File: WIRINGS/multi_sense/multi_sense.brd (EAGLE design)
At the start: 45.7 x 62.2 mm, 7 parts

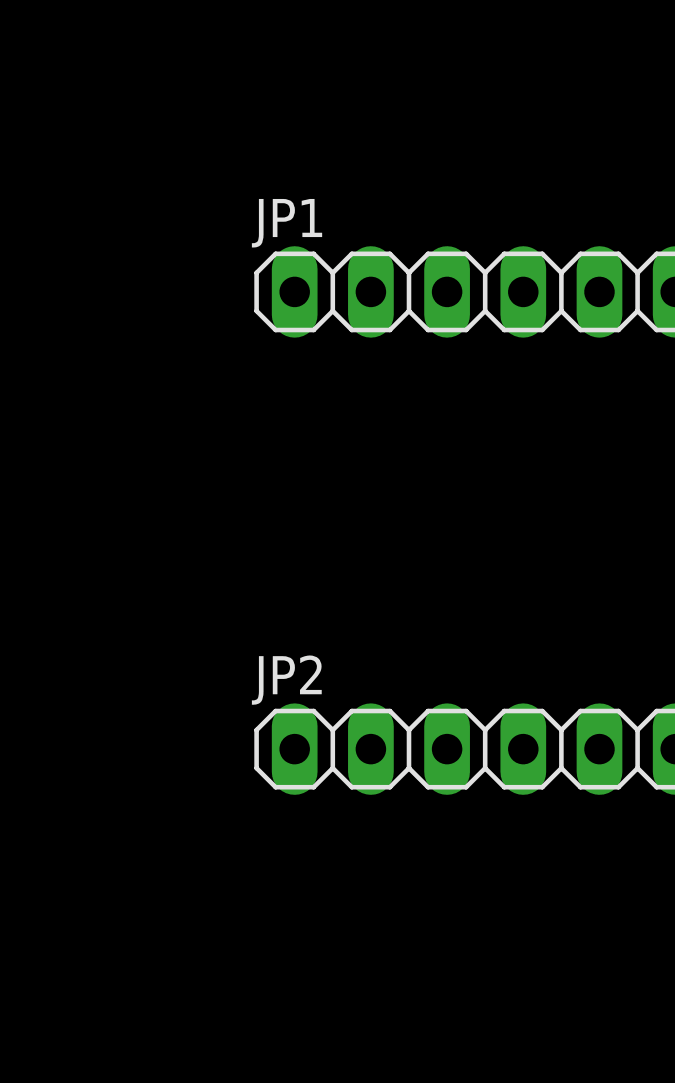
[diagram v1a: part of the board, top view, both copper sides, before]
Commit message: updated wemos and diverse boards
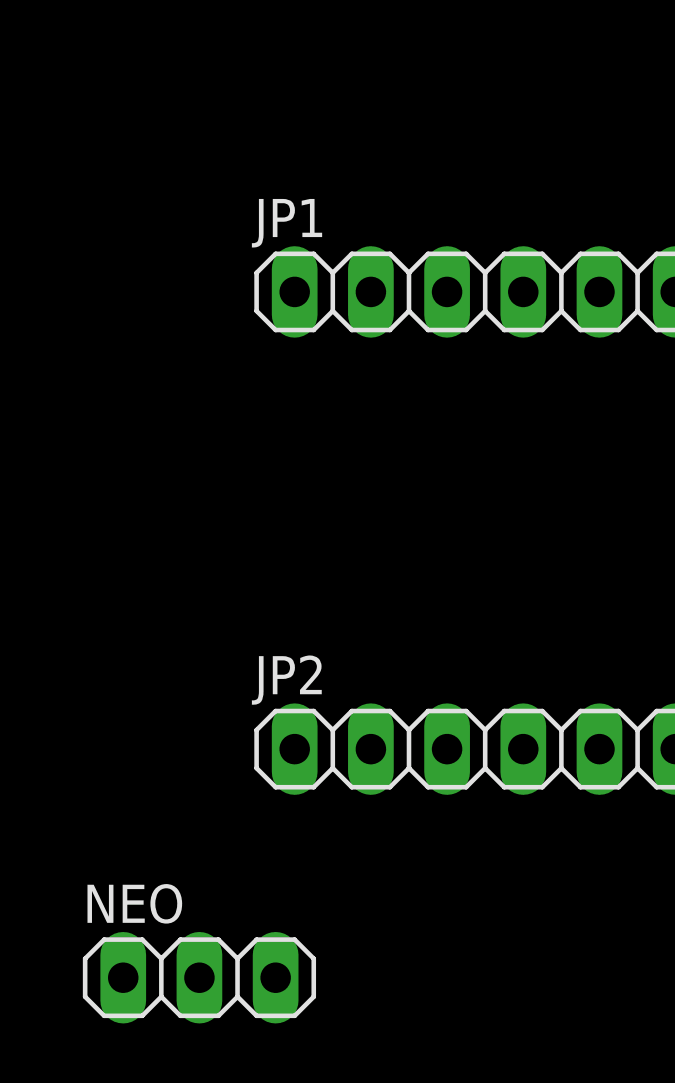
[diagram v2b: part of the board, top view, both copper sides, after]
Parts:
- added NEO: (no value), pinhead:1X03
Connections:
- new net NEOGND: NEO.2
- new net NEOPWR: NEO.3
- new net NEOSIG: NEO.1
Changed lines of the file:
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@@
 <?xml version="1.0" encoding="utf-8"?>
 <!DOCTYPE eagle SYSTEM "eagle.dtd">
-<eagle version="8.3.2">
+<eagle version="9.6.2">
 <drawing>
 <settings>
@@
 <param name="dpMaxLengthDifference" value="10mm"/>
 <param name="dpGapFactor" value="2.5"/>
-<param name="checkGrid" value="0"/>
 <param name="checkAngle" value="0"/>
 <param name="checkFont" value="1"/>
 <param name="checkRestrict" value="0"/>
+<param name="checkStop" value="0"/>
+<param name="checkValues" value="0"/>
+<param name="checkNames" value="1"/>
+<param name="checkWireStubs" value="1"/>
+<param name="checkPolygonWidth" value="0"/>
 <param name="useDiameter" value="13"/>
 <param name="maxErrors" value="50"/>
@@
 </autorouter>
 <elements>
-<element name="U$2" library="BRAND_SWI" package="BRAND_SWI_5X7" value="" x="11.303" y="0.635" rot="MR0"/>
-<element name="R1" library="rcl" library_urn="urn:adsk.eagle:library:334" package="0207/10" package3d_urn="urn:adsk.eagle:package:23491/1" value="10k" x="10.795" y="-130.81"/>
-<element name="PIR" library="pinhead" library_urn="urn:adsk.eagle:library:325" package="1X03" package3d_urn="urn:adsk.eagle:package:22458/2" value="" x="10.16" y="-290.83"/>
-<element name="DHT" library="pinhead" library_urn="urn:adsk.eagle:library:325" package="1X04" package3d_urn="urn:adsk.eagle:package:22407/2" value="" x="11.43" y="-306.07"/>
-<element name="TEMT6000" library="pinhead" library_urn="urn:adsk.eagle:library:325" package="1X03" package3d_urn="urn:adsk.eagle:package:22458/2" value="" x="10.16" y="-321.31"/>
-<element name="JP1" library="pinhead" library_urn="urn:adsk.eagle:library:325" package="1X15" package3d_urn="urn:adsk.eagle:package:22424/1" value="ESP8266_LEFT" x="25.4" y="-336.55"/>
-<element name="JP2" library="pinhead" library_urn="urn:adsk.eagle:library:325" package="1X15" package3d_urn="urn:adsk.eagle:package:22424/1" value="ESP8266_LEFT" x="25.4" y="-351.79"/>
+<element name="U$2" library="BRAND_SWI" package="BRAND_SWI_5X7" value="" x="11.303" y="0.635" smashed="yes" rot="MR0"/>
+<element name="R1" library="rcl" library_urn="urn:adsk.eagle:library:334" package="0207/10" package3d_urn="urn:adsk.eagle:package:23491/1" value="10k" x="10.795" y="-130.81" smashed="yes">
+<attribute name="NAME" x="7.747" y="-129.286" size="1.27" layer="25" ratio="10"/>
+<attribute name="VALUE" x="8.5344" y="-131.445" size="1.27" layer="27" ratio="10"/>
+</element>
+<element name="PIR" library="pinhead" library_urn="urn:adsk.eagle:library:325" package="1X03" package3d_urn="urn:adsk.eagle:package:22458/2" value="" x="10.16" y="-290.83" smashed="yes">
+<attribute name="NAME" x="6.2738" y="-289.0012" size="1.27" layer="25" ratio="10"/>
+<attribute name="VALUE" x="6.35" y="-294.005" size="1.27" layer="27"/>
+</element>
+<element name="DHT" library="pinhead" library_urn="urn:adsk.eagle:library:325" package="1X04" package3d_urn="urn:adsk.eagle:package:22407/2" value="" x="11.43" y="-306.07" smashed="yes">
+<attribute name="NAME" x="6.2738" y="-304.2412" size="1.27" layer="25" ratio="10"/>
+<attribute name="VALUE" x="6.35" y="-309.245" size="1.27" layer="27"/>
+</element>
+<element name="TEMT6000" library="pinhead" library_urn="urn:adsk.eagle:library:325" package="1X03" package3d_urn="urn:adsk.eagle:package:22458/2" value="" x="10.16" y="-321.31" smashed="yes">
+<attribute name="NAME" x="6.2738" y="-319.4812" size="1.27" layer="25" ratio="10"/>
+<attribute name="VALUE" x="6.35" y="-324.485" size="1.27" layer="27"/>
+</element>
+<element name="JP1" library="pinhead" library_urn="urn:adsk.eagle:library:325" package="1X15" package3d_urn="urn:adsk.eagle:package:22424/1" value="ESP8266_LEFT" x="25.4" y="-336.55" smashed="yes">
+<attribute name="NAME" x="6.2738" y="-334.7212" size="1.27" layer="25" ratio="10"/>
+<attribute name="VALUE" x="6.35" y="-339.725" size="1.27" layer="27"/>
+</element>
+<element name="JP2" library="pinhead" library_urn="urn:adsk.eagle:library:325" package="1X15" package3d_urn="urn:adsk.eagle:package:22424/1" value="ESP8266_LEFT" x="25.4" y="-351.79" smashed="yes">
+<attribute name="NAME" x="6.2738" y="-349.9612" size="1.27" layer="25" ratio="10"/>
+<attribute name="VALUE" x="6.35" y="-354.965" size="1.27" layer="27"/>
+</element>
+<element name="NEO" library="pinhead" library_urn="urn:adsk.eagle:library:325" package="1X03" package3d_urn="urn:adsk.eagle:package:22458/2" value="" x="4.445" y="-359.41" smashed="yes">
+<attribute name="NAME" x="0.5588" y="-357.5812" size="1.27" layer="25" ratio="10"/>
+<attribute name="VALUE" x="0.635" y="-362.585" size="1.27" layer="27"/>
+</element>
 </elements>
 <signals>
@@
 <contactref element="R1" pad="2"/>
 </signal>
+<signal name="NEOSIG">
+<contactref element="NEO" pad="1"/>
+</signal>
+<signal name="NEOGND">
+<contactref element="NEO" pad="2"/>
+</signal>
+<signal name="NEOPWR">
+<contactref element="NEO" pad="3"/>
+</signal>
 </signals>
+<mfgpreviewcolors>
+<mfgpreviewcolor name="soldermaskcolor" color="0xC8008000"/>
+<mfgpreviewcolor name="silkscreencolor" color="0xFFFEFEFE"/>
+<mfgpreviewcolor name="backgroundcolor" color="0xFF282828"/>
+<mfgpreviewcolor name="coppercolor" color="0xFFFFBF00"/>
+<mfgpreviewcolor name="substratecolor" color="0xFF786E46"/>
+</mfgpreviewcolors>
 </board>
 </drawing>
